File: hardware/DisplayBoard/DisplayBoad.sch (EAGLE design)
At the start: 45 parts, among them IC1 MCP23017, SW1 EC12E_SW, SW2 EC12E_SW, U1 EADOGL128-6

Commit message: Updates
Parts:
- U1: value EADOGL128-6 -> EADOGL128-62; device ea:EADOGL128-6 -> ea:EADOGL128-62
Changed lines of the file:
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@@
 </classes>
 <parts>
-<part name="U1" library="ea" deviceset="EADOGL128-6" device=""/>
+<part name="U1" library="ea" deviceset="EADOGL128-6" device="2" value="EADOGL128-62"/>
 <part name="SW1" library="switch-alps" deviceset="EC12E_SW" device=""/>
 <part name="C1" library="resistor" deviceset="C-EU" device="C0805" value="1u"/>

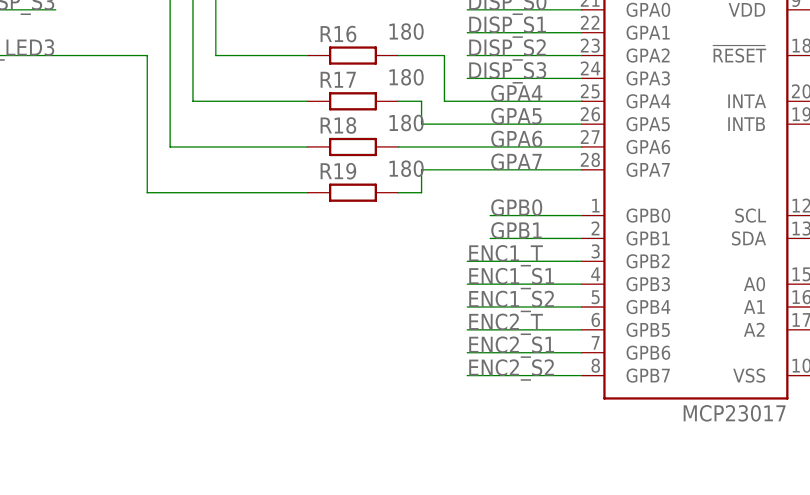
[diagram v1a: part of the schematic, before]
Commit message: Ordered Version
Small mechanical changes
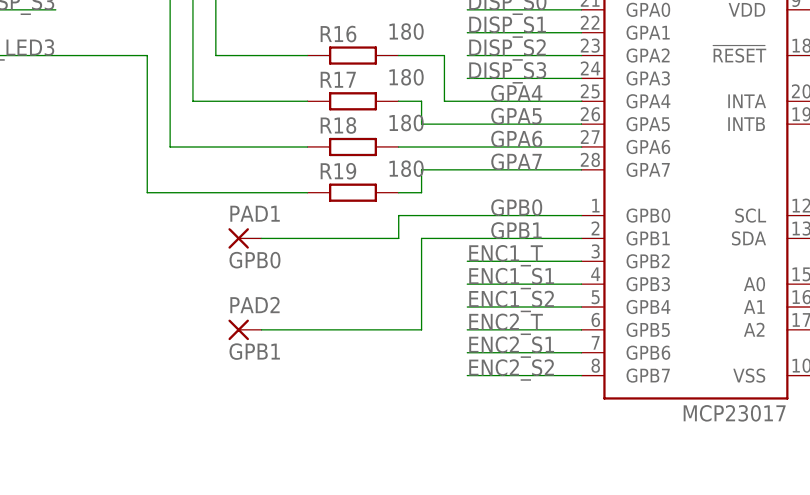
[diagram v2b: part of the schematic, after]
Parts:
- added PAD1: GPB0, wirepad:2,15/1,0
- added PAD2: GPB1, wirepad:2,15/1,0
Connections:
- net GPB0: now also PAD1.P
- net GPB1: now also PAD2.P
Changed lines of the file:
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@@
 <part name="C16" library="resistor" deviceset="C-EU" device="C0603" value="100n"/>
 <part name="GND10" library="supply1" deviceset="GND" device=""/>
+<part name="PAD1" library="wirepad" deviceset="2,15/1,0" device="" value="GPB0"/>
+<part name="PAD2" library="wirepad" deviceset="2,15/1,0" device="" value="GPB1"/>
 </parts>
 <sheets>
@@
 <instance part="C16" gate="G$1" x="147.32" y="83.82" rot="R180"/>
 <instance part="GND10" gate="1" x="147.32" y="93.98" rot="R180"/>
+<instance part="PAD1" gate="1" x="76.2" y="53.34"/>
+<instance part="PAD2" gate="1" x="76.2" y="43.18"/>
 </instances>
 <busses>
@@
 <segment>
 <pinref part="IC1" gate="G$1" pin="GPB0"/>
-<wire x1="114.3" y1="55.88" x2="104.14" y2="55.88" width="0.1524" layer="91"/>
 <label x="104.14" y="55.88" size="1.778" layer="95"/>
+<pinref part="PAD1" gate="1" pin="P"/>
+<wire x1="78.74" y1="53.34" x2="93.98" y2="53.34" width="0.1524" layer="91"/>
+<wire x1="93.98" y1="53.34" x2="93.98" y2="55.88" width="0.1524" layer="91"/>
+<wire x1="93.98" y1="55.88" x2="114.3" y2="55.88" width="0.1524" layer="91"/>
 </segment>
 </net>
@@
 <segment>
 <pinref part="IC1" gate="G$1" pin="GPB1"/>
-<wire x1="114.3" y1="53.34" x2="104.14" y2="53.34" width="0.1524" layer="91"/>
+<wire x1="114.3" y1="53.34" x2="96.52" y2="53.34" width="0.1524" layer="91"/>
 <label x="104.14" y="53.34" size="1.778" layer="95"/>
-</segment>
-</net>
+<wire x1="96.52" y1="53.34" x2="96.52" y2="43.18" width="0.1524" layer="91"/>
+<pinref part="PAD2" gate="1" pin="P"/>
+<wire x1="96.52" y1="43.18" x2="78.74" y2="43.18" width="0.1524" layer="91"/>
+</segment>
+</net>

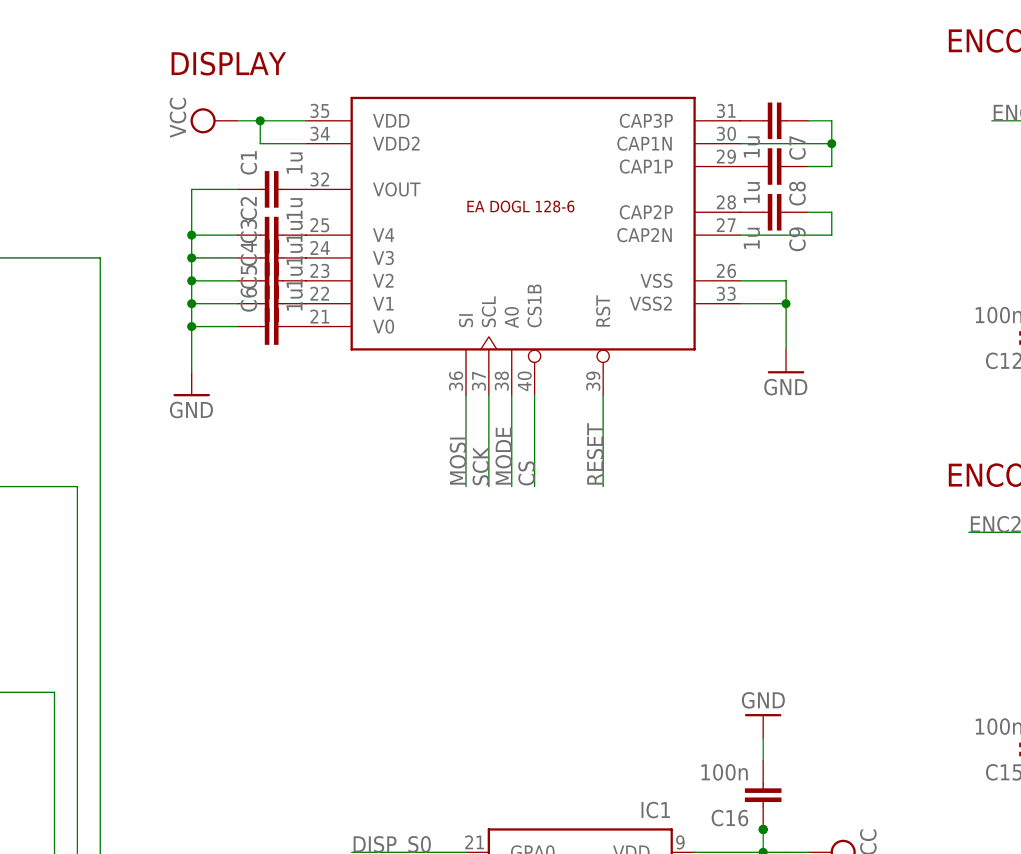
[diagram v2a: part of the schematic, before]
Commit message: DisplayBoard: missing connections
Design error: missing pwr connections for display backlight.
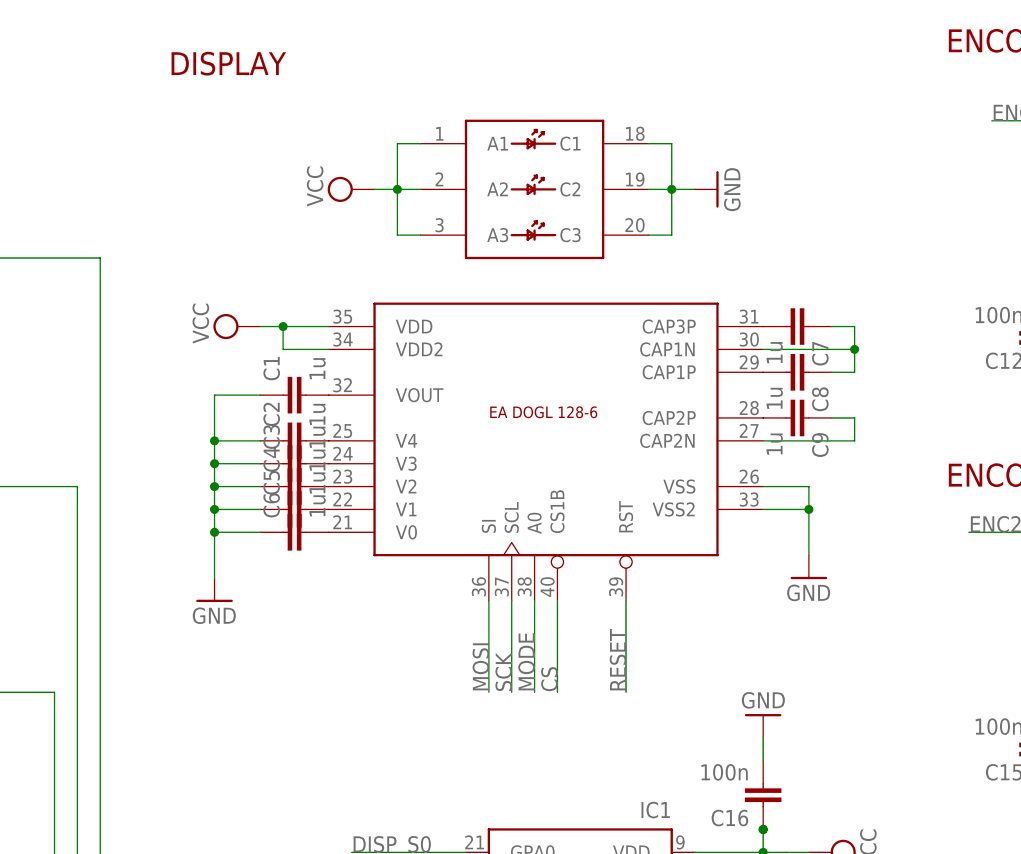
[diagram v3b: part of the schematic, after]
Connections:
- net CS: now also U1G$1.CS1B; no longer U1.CS1B
- net GND: now also U1G$1.VSS, U1G$1.VSS2, U1G$2.C1, U1G$2.C2, U1G$2.C3; no longer U1.VSS, U1.VSS2
- net MODE: now also U1G$1.A0; no longer U1.A0
- net MOSI: now also U1G$1.SI; no longer U1.SI
- net N$1: now also U1G$1.VOUT; no longer U1.VOUT
- net N$10: now also U1G$1.CAP2N; no longer U1.CAP2N
- net N$11: now also U1G$1.CAP1N; no longer U1.CAP1N
- net N$2: now also U1G$1.V4; no longer U1.V4
- net N$3: now also U1G$1.V3; no longer U1.V3
- net N$4: now also U1G$1.V2; no longer U1.V2
- net N$5: now also U1G$1.V1; no longer U1.V1
- net N$6: now also U1G$1.V0; no longer U1.V0
- net N$7: now also U1G$1.CAP3P; no longer U1.CAP3P
- net N$8: now also U1G$1.CAP1P; no longer U1.CAP1P
- net N$9: now also U1G$1.CAP2P; no longer U1.CAP2P
- net RESET: now also U1G$1.RST; no longer U1.RST
- net SCK: now also U1G$1.SCL; no longer U1.SCL
- net VCC: now also U1G$1.VDD, U1G$1.VDD2, U1G$2.A1, U1G$2.A2, U1G$2.A3; no longer U1.VDD, U1.VDD2
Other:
- moved on the sheet: C1, C2, C3, C4, C5, C6, C7, C8, C9
